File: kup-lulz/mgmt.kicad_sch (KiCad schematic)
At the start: 25 parts, among them J14 PMOD_HOST, J37 XILINX_JTAG, J38 PMOD_HOST, J39 CONN_01X03, U14 STM32L431VxIx, U15 AT24MAC402, U9 XILINX_ULTRASCALEPLUS_B676

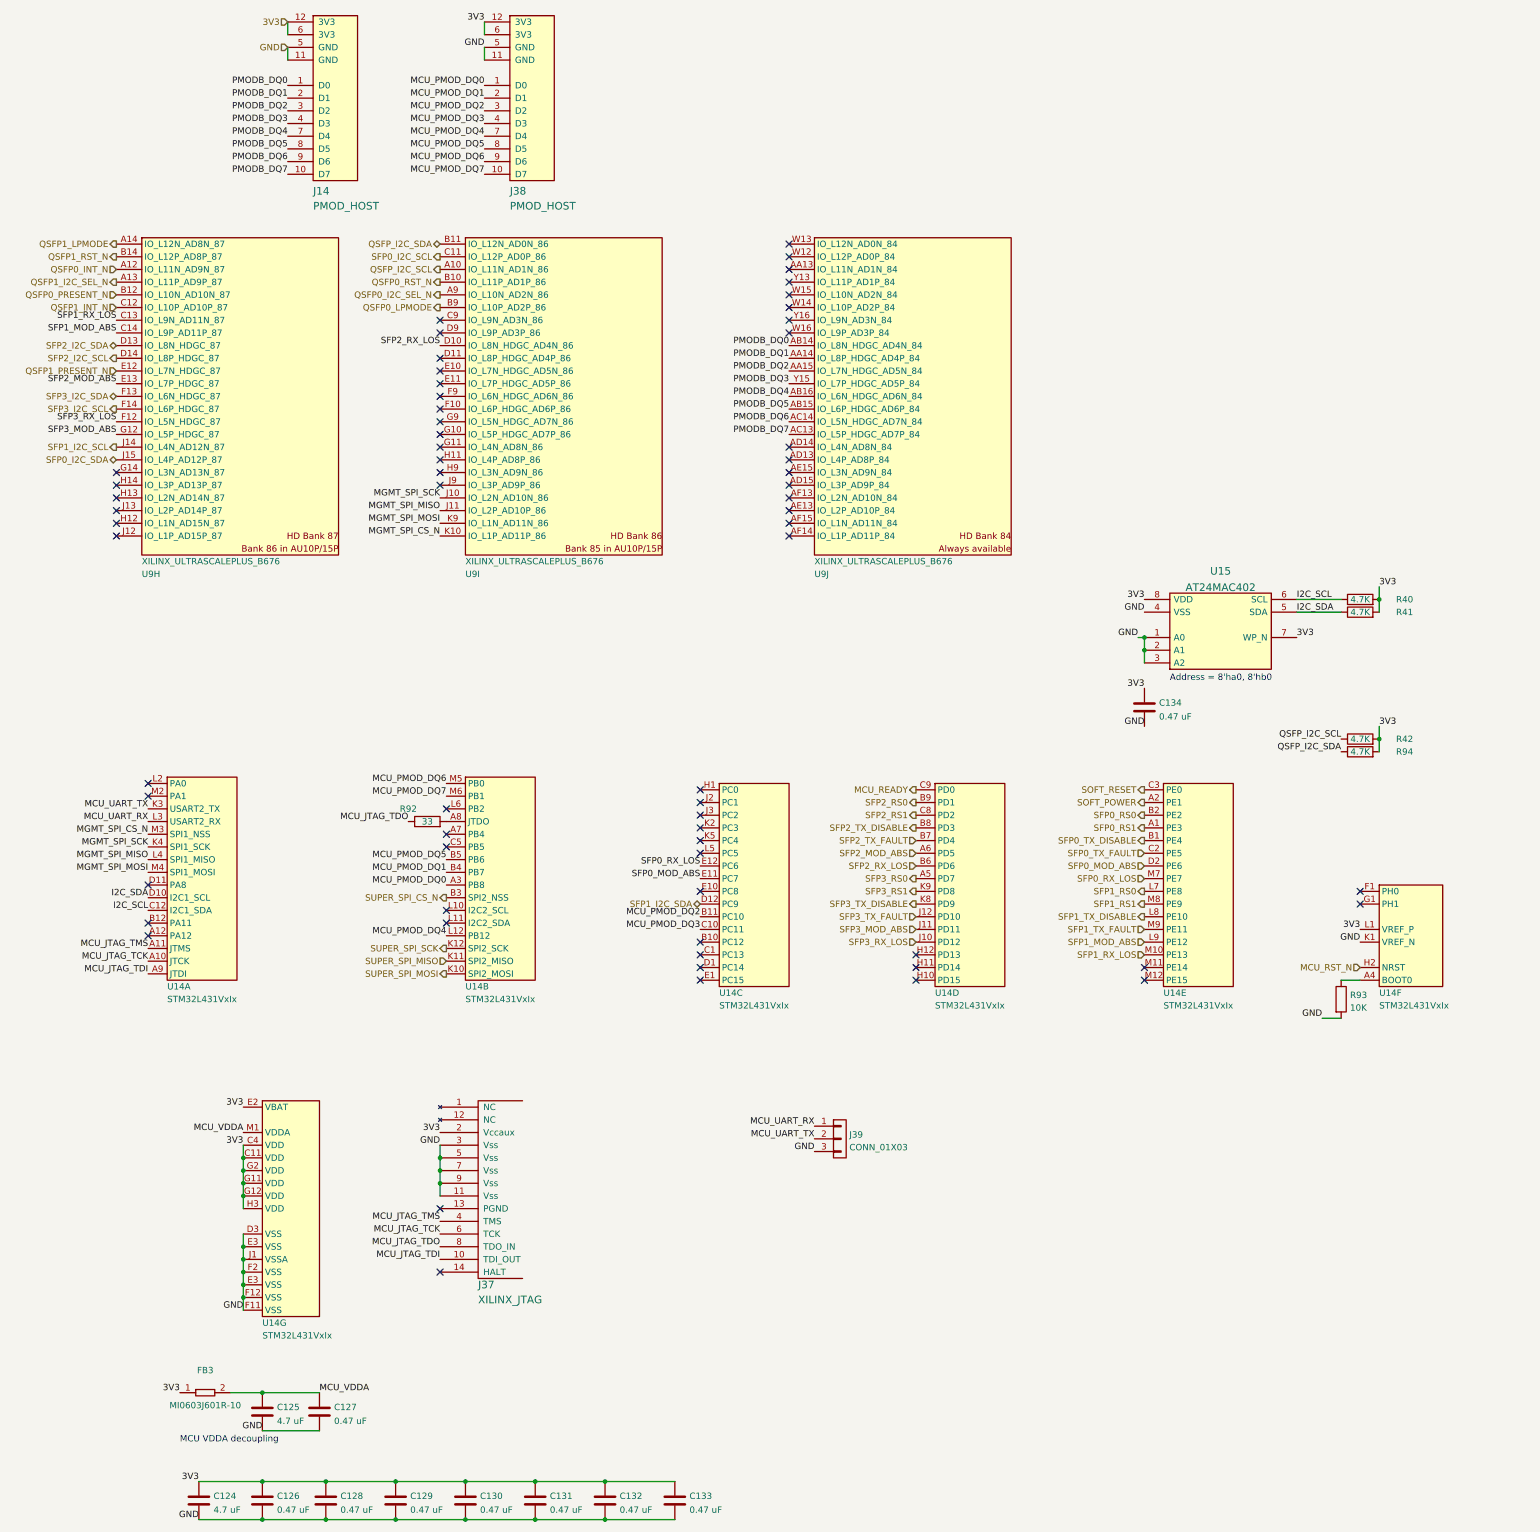
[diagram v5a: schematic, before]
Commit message: FPGA is fully scaped, maybe? just need to hook up MCU now
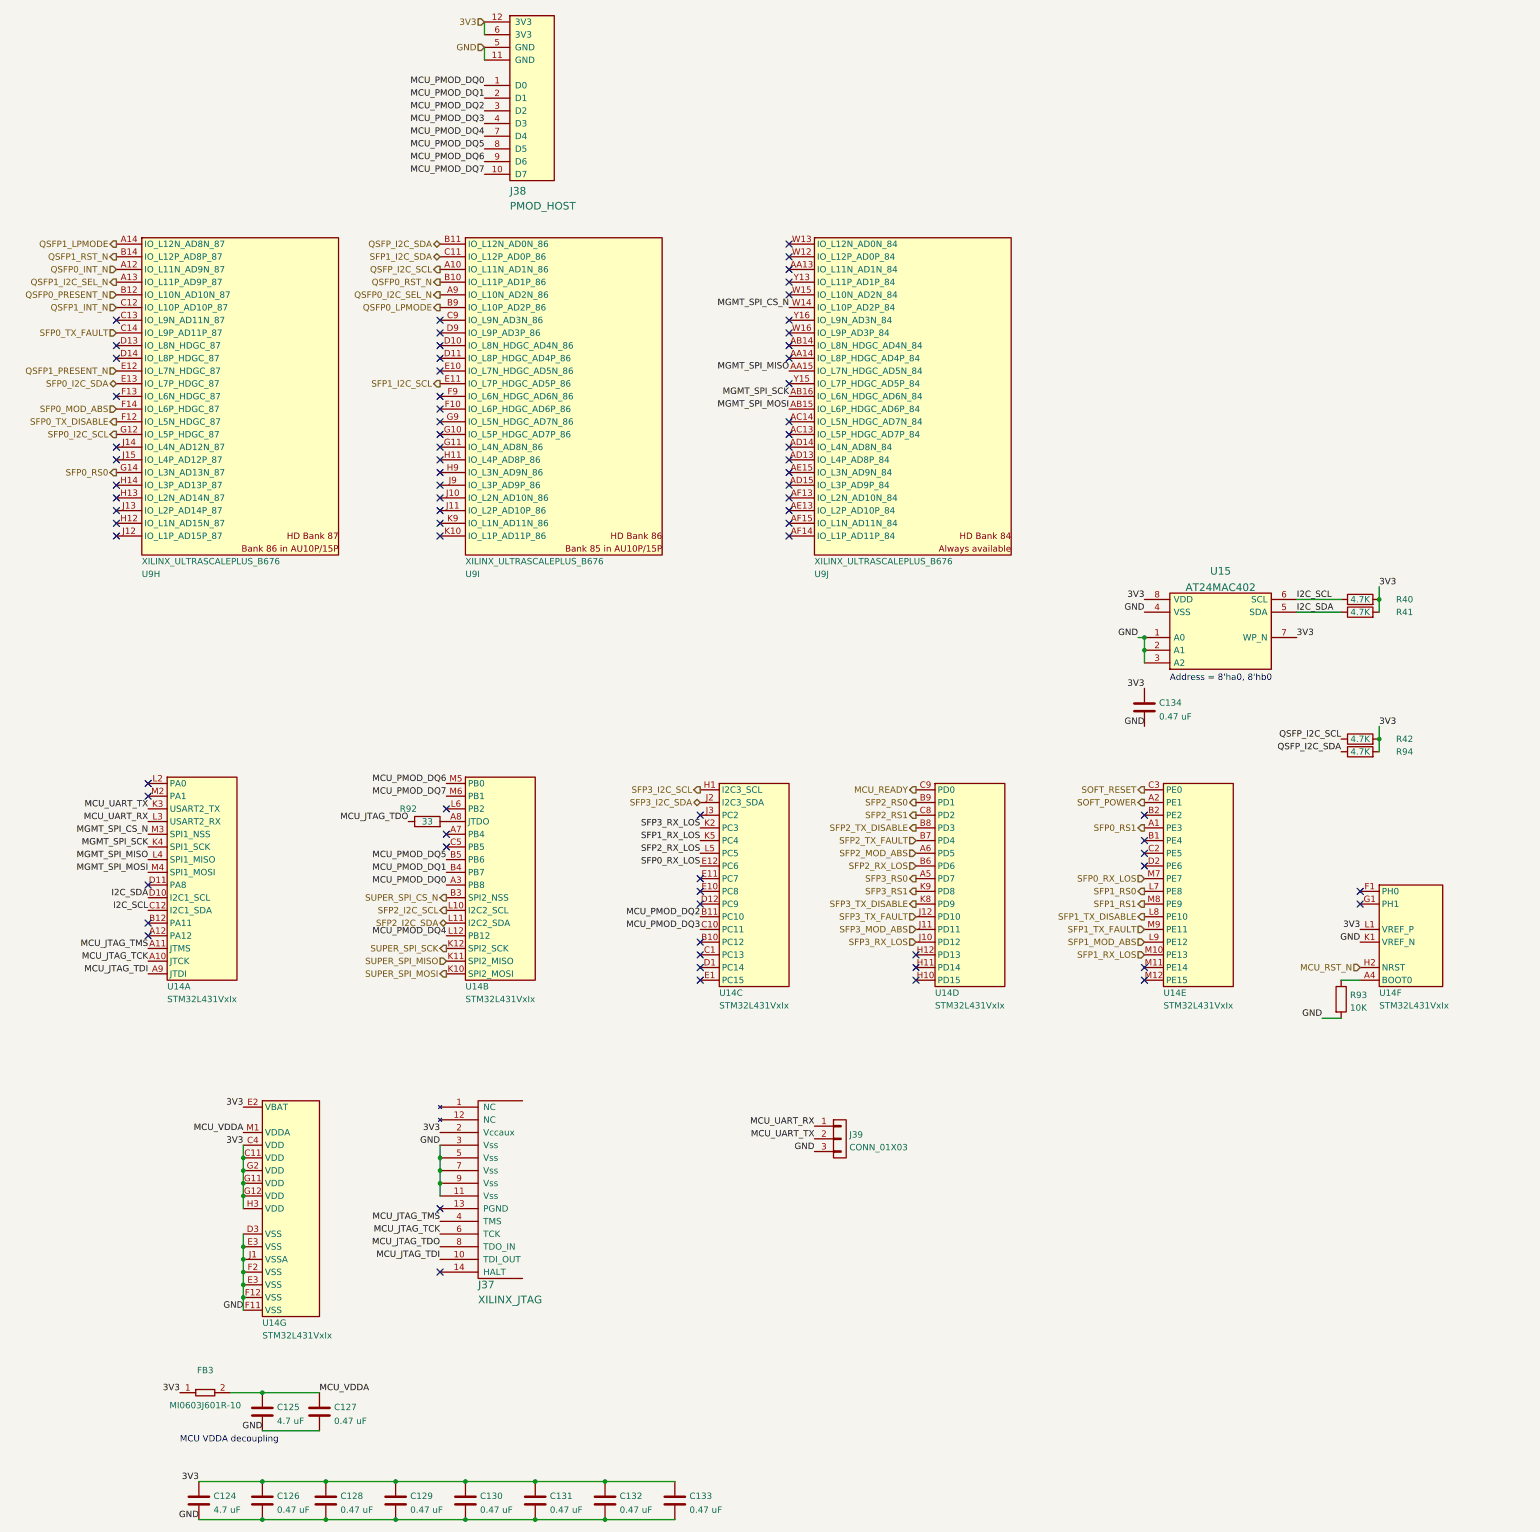
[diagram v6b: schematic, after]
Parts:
- removed J14: PMOD_HOST, azonenberg_pcb:CONN_HEADER_2.54MM_2x6_RA_PMOD_HOST, symbol special-azonenberg:PMOD_HOST
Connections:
- net PMODB_DQ2 is gone; now on net MGMT_SPI_MISO: U9.AA15 (IO_L7N_HDGC_AD5N_84)
- net PMODB_DQ4 is gone; now on net MGMT_SPI_SCK: U9.AB16 (IO_L6N_HDGC_AD6N_84)
- net PMODB_DQ5 is gone; now on net MGMT_SPI_MOSI: U9.AB15 (IO_L6P_HDGC_AD6P_84)
- net MGMT_SPI_CS_N: now also U9.W14 (IO_L10P_AD2P_84); no longer U9.K10 (IO_L1P_AD11P_86)
- net MGMT_SPI_MISO: no longer U9.J11 (IO_L2P_AD10P_86)
- net MGMT_SPI_MOSI: no longer U9.K9 (IO_L1N_AD11N_86)
- net MGMT_SPI_SCK: no longer U9.J10 (IO_L2N_AD10N_86)
- net SFP0_I2C_SCL: now also U9.G12 (IO_L5P_HDGC_87); no longer U9.C11 (IO_L12P_AD0P_86)
- net SFP0_I2C_SDA: now also U9.E13 (IO_L7P_HDGC_87); no longer U9.J15 (IO_L4P_AD12P_87)
- net SFP0_MOD_ABS: now also U9.F14 (IO_L6P_HDGC_87); no longer U14.D2 (PE6), U14.E11 (PC7)
- net SFP0_RS0: now also U9.G14 (IO_L3N_AD13N_87); no longer U14.B2 (PE2)
- net SFP0_TX_DISABLE: now also U9.F12 (IO_L5N_HDGC_87); no longer U14.B1 (PE4)
- net SFP0_TX_FAULT: now also U9.C14 (IO_L9P_AD11P_87); no longer U14.C2 (PE5)
- net SFP1_I2C_SCL: now also U9.E11 (IO_L7P_HDGC_AD5P_86); no longer U9.J14 (IO_L4N_AD12N_87)
- net SFP1_I2C_SDA: now also U9.C11 (IO_L12P_AD0P_86); no longer U14.D12 (PC9)
- net SFP1_MOD_ABS: no longer U9.C14 (IO_L9P_AD11P_87)
- net SFP1_RX_LOS: now also U14.K5 (PC4); no longer U9.C13 (IO_L9N_AD11N_87)
- net SFP2_I2C_SCL: now also U14.L10 (PB10); no longer U9.D14 (IO_L8P_HDGC_87)
- net SFP2_I2C_SDA: now also U14.L11 (PB11); no longer U9.D13 (IO_L8N_HDGC_87)
- net SFP2_MOD_ABS: no longer U9.E13 (IO_L7P_HDGC_87)
- net SFP2_RX_LOS: now also U14.L5 (PC5); no longer U9.D10 (IO_L8N_HDGC_AD4N_86)
- net SFP3_I2C_SCL: now also U14.H1 (PC0); no longer U9.F14 (IO_L6P_HDGC_87)
- net SFP3_I2C_SDA: now also U14.J2 (PC1); no longer U9.F13 (IO_L6N_HDGC_87)
- net SFP3_MOD_ABS: no longer U9.G12 (IO_L5P_HDGC_87)
- net SFP3_RX_LOS: now also U14.K2 (PC3); no longer U9.F12 (IO_L5N_HDGC_87)
- net PMODB_DQ0: no longer names the net of U9.AB14 (IO_L8N_HDGC_AD4N_84)
- net PMODB_DQ1: no longer names the net of U9.AA14 (IO_L8P_HDGC_AD4P_84)
- net PMODB_DQ3: no longer names the net of U9.Y15 (IO_L7P_HDGC_AD5P_84)
- net PMODB_DQ6: no longer names the net of U9.AC14 (IO_L5N_HDGC_AD7N_84)
- net PMODB_DQ7: no longer names the net of U9.AC13 (IO_L5P_HDGC_AD7P_84)
- no-connect marks 65 -> 77

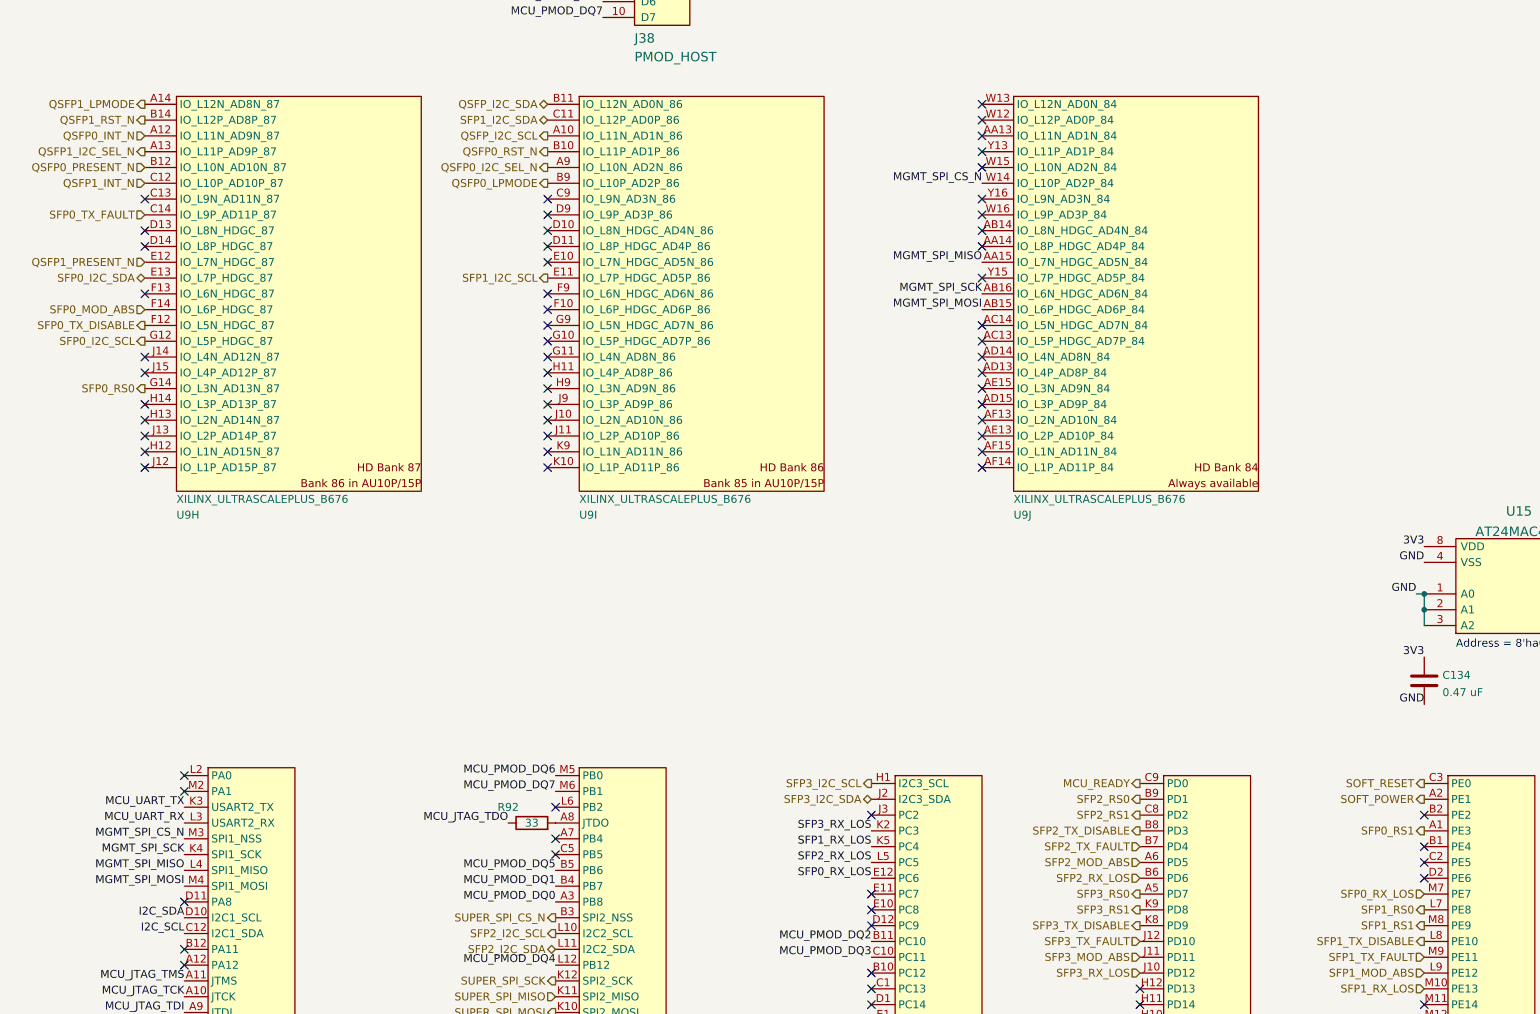
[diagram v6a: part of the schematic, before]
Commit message: kup-lulz: continued initial layout, moved SFP0 GPIOs to be entirely FPGA driven
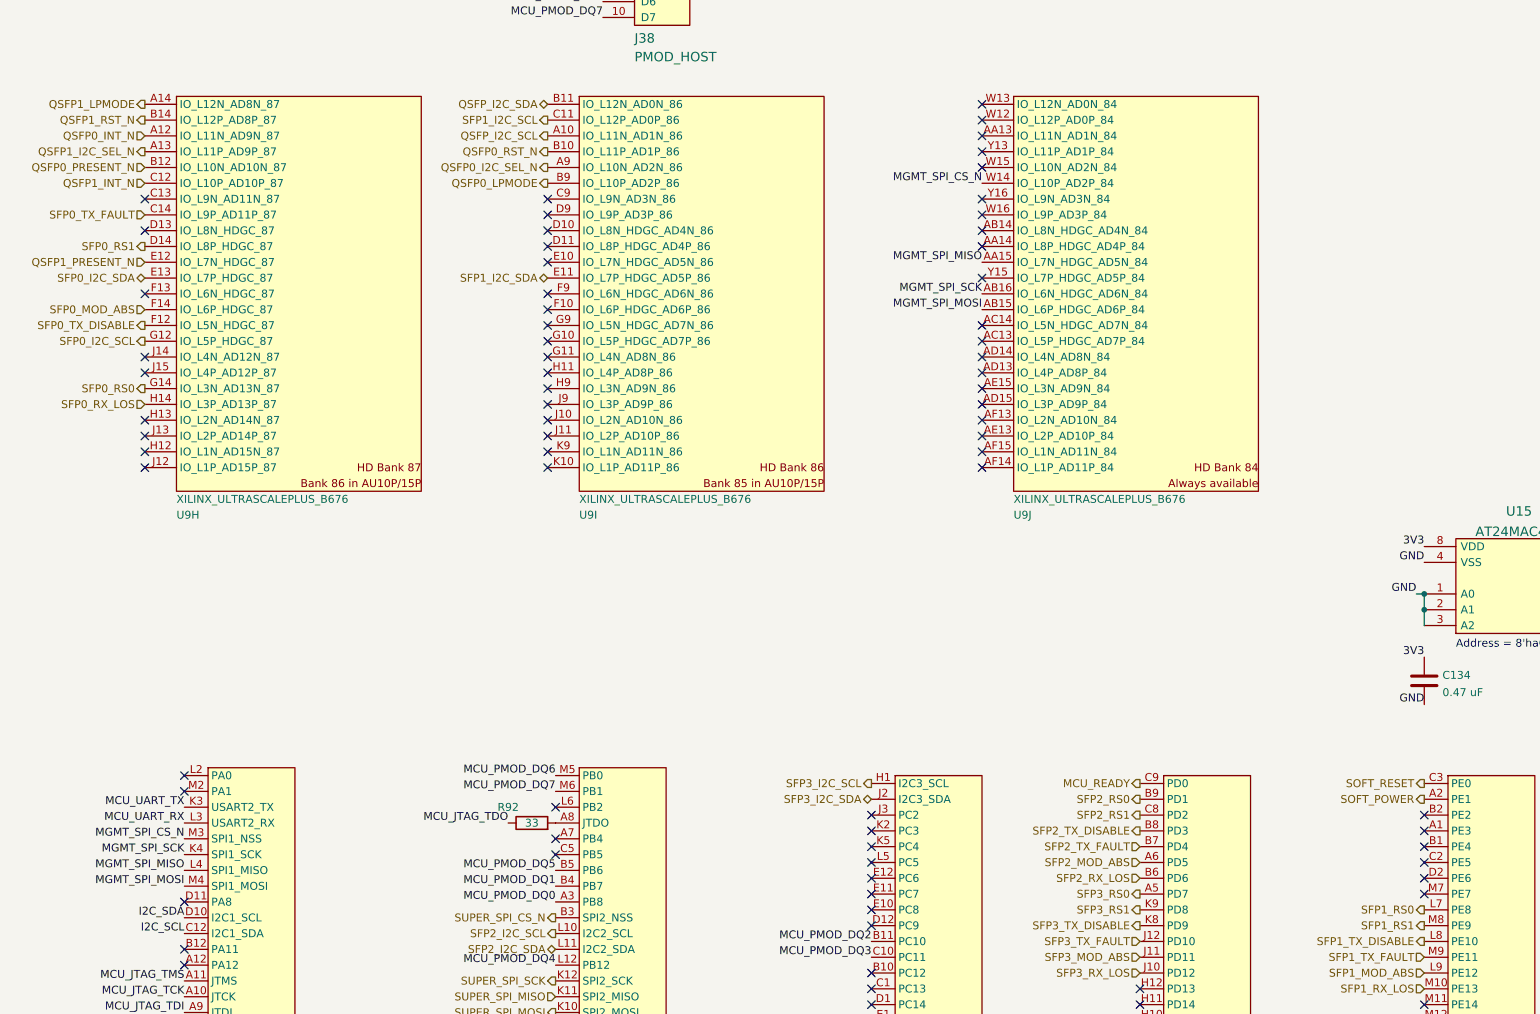
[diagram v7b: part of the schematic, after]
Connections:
- net SFP0_RS1: now also U9.D14 (IO_L8P_HDGC_87); no longer U14.A1 (PE3)
- net SFP0_RX_LOS: now also U9.H14 (IO_L3P_AD13P_87); no longer U14.E12 (PC6), U14.M7 (PE7)
- net SFP1_I2C_SCL: now also U9.C11 (IO_L12P_AD0P_86); no longer U9.E11 (IO_L7P_HDGC_AD5P_86)
- net SFP1_I2C_SDA: now also U9.E11 (IO_L7P_HDGC_AD5P_86); no longer U9.C11 (IO_L12P_AD0P_86)
- net SFP1_RX_LOS: no longer U14.K5 (PC4)
- net SFP2_RX_LOS: no longer U14.L5 (PC5)
- net SFP3_RX_LOS: no longer U14.K2 (PC3)
- no-connect marks 77 -> 81
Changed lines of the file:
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@@
   (title_block
     (title "Kintex Ultrascale+ OshPark For The Lulz")
-    (date "2024-02-08")
+    (date "2024-02-21")
     (rev "0.1")
     (company "Antikernel Labs")
@@
   )
   (no_connect (at 196.85 204.47))
+  (no_connect (at 153.67 184.15))
   (no_connect (at 171.45 102.87))
   (no_connect (at 171.45 72.39))
@@
   (no_connect (at 101.6 120.65))
   (no_connect (at 101.6 95.25))
+  (no_connect (at 242.57 179.07))
   (no_connect (at 196.85 209.55))
   (no_connect (at 171.45 85.09))
@@
   (no_connect (at 101.6 92.71))
   (no_connect (at 101.6 97.79))
+  (no_connect (at 153.67 181.61))
   (no_connect (at 36.83 120.65))
   (no_connect (at 101.6 113.03))
@@
   (no_connect (at 242.57 176.53))
   (no_connect (at 171.45 110.49))
-  (no_connect (at 36.83 85.09))
+  (no_connect (at 153.67 186.69))
   (no_connect (at 153.67 194.31))
   (no_connect (at 171.45 90.17))
@@
   (no_connect (at 242.57 181.61))
   (no_connect (at 101.6 115.57))
+  (no_connect (at 242.57 189.23))
   (no_connect (at 36.83 105.41))
   (no_connect (at 101.6 77.47))
   (no_connect (at 242.57 186.69))
   (no_connect (at 36.83 113.03))
-  (no_connect (at 36.83 110.49))
   (no_connect (at 171.45 115.57))
   (no_connect (at 171.45 80.01))
@@
   (no_connect (at 171.45 100.33))
   (no_connect (at 171.45 77.47))
+  (no_connect (at 153.67 179.07))
   (no_connect (at 36.83 115.57))
   (no_connect (at 171.45 113.03))
@@
     (effects (font (size 1.27 1.27)) (justify right bottom))
   )
-  (label "SFP1_RX_LOS" (at 153.67 181.61 180)
-    (effects (font (size 1.27 1.27)) (justify right bottom))
-  )
   (label "MCU_JTAG_TCK" (at 101.6 260.35 180)
     (effects (font (size 1.27 1.27)) (justify right bottom))
@@
     (effects (font (size 1.27 1.27)) (justify right bottom))
   )
-  (label "SFP3_RX_LOS" (at 153.67 179.07 180)
-    (effects (font (size 1.27 1.27)) (justify right bottom))
-  )
   (label "3V3" (at 62.23 234.95 180)
     (effects (font (size 1.27 1.27)) (justify right bottom))
@@
     (effects (font (size 1.27 1.27)) (justify left bottom))
   )
-  (label "SFP2_RX_LOS" (at 153.67 184.15 180)
-    (effects (font (size 1.27 1.27)) (justify right bottom))
-  )
   (label "MCU_JTAG_TDI" (at 43.18 208.28 180)
     (effects (font (size 1.27 1.27)) (justify right bottom))
@@
     (effects (font (size 1.27 1.27)) (justify left bottom))
   )
-  (label "SFP0_RX_LOS" (at 153.67 186.69 180)
-    (effects (font (size 1.27 1.27)) (justify right bottom))
-  )
   (label "MGMT_SPI_MISO" (at 43.18 185.42 180)
     (effects (font (size 1.27 1.27)) (justify right bottom))
@@
     (effects (font (size 1.27 1.27)) (justify right))
   )
-  (hierarchical_label "SFP0_RS1" (shape output) (at 242.57 179.07 180)
+  (hierarchical_label "SFP0_RS1" (shape output) (at 36.83 85.09 180)
     (effects (font (size 1.27 1.27)) (justify right))
   )
@@
     (effects (font (size 1.27 1.27)) (justify right))
   )
-  (hierarchical_label "SFP1_I2C_SDA" (shape bidirectional) (at 101.6 64.77 180)
+  (hierarchical_label "SFP1_I2C_SDA" (shape bidirectional) (at 101.6 90.17 180)
     (effects (font (size 1.27 1.27)) (justify right))
   )
@@
     (effects (font (size 1.27 1.27)) (justify right))
   )
-  (hierarchical_label "SFP0_RX_LOS" (shape input) (at 242.57 189.23 180)
+  (hierarchical_label "SFP0_RX_LOS" (shape input) (at 36.83 110.49 180)
     (effects (font (size 1.27 1.27)) (justify right))
   )
@@
     (effects (font (size 1.27 1.27)) (justify right))
   )
-  (hierarchical_label "SFP1_I2C_SCL" (shape output) (at 101.6 90.17 180)
-    (effects (font (size 1.27 1.27)) (justify right))
-  )
+  (hierarchical_label "SFP1_I2C_SCL" (shape output) (at 101.6 64.77 180)
+    (effects (font (size 1.27 1.27)) (justify right))
+  )
